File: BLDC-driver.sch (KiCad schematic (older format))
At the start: 80 parts, among them J1 Conn_01x06, J2 Conn_01x06, Q1 FDMS8018, Q2 FDMS8018, Q3 FDMS8018, Q4 FDMS8018, Q5 FDMS8018, Q6 FDMS8018, U1 NCP81151B, U2 STM32F103C8Tx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

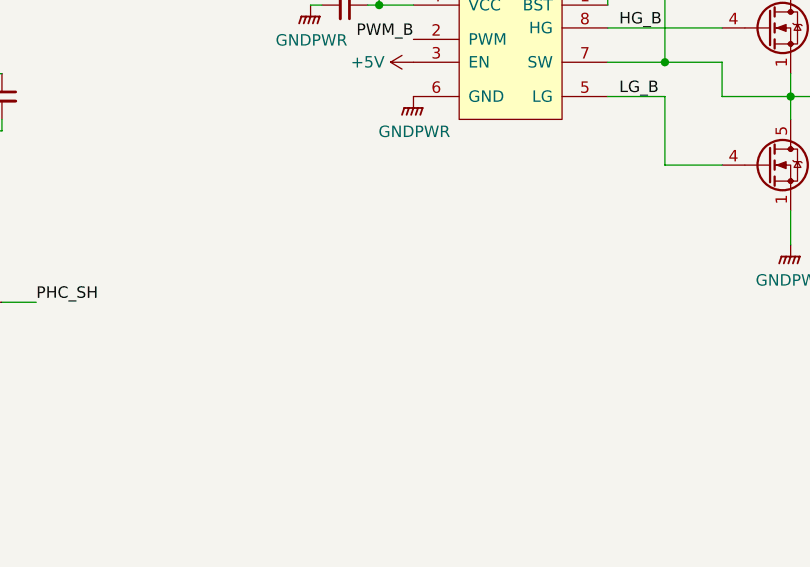
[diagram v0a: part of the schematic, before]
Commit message: add pwm 5v pull up
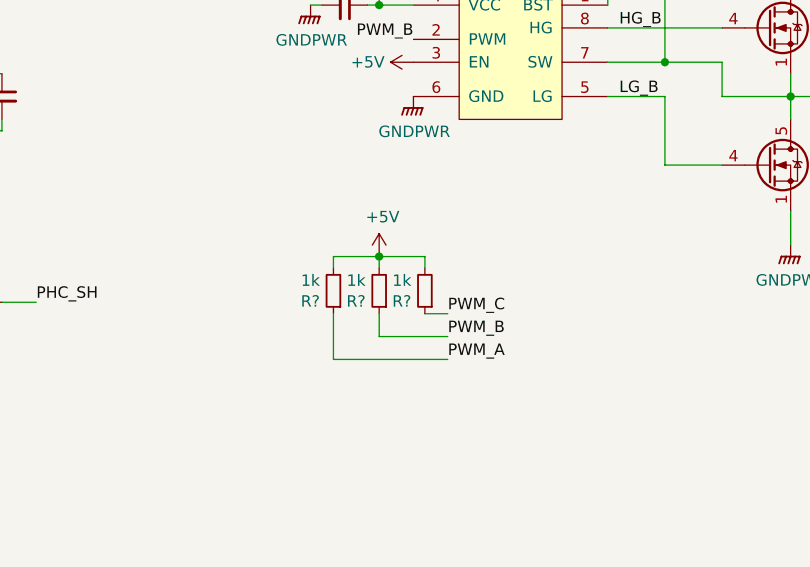
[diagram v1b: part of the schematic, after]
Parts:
- added R? (x3): 1k, Resistor_SMD:R_0402_1005Metric, symbol Device:R_Small
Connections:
- wire segments 294 -> 304
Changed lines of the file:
@@
+	1    0    0    -1
+$EndComp
+Text Label 8400 6250 0    50   ~ 0
+PWM_C
+Text Label 8400 6350 0    50   ~ 0
+PWM_B
+Text Label 8400 6450 0    50   ~ 0
+PWM_A
+$Comp
+L Device:R_Small R?
+U 1 1 5F02E223
+P 8300 6150
+F 0 "R?" H 8359 6196 50  0000 L CNN
+F 1 "1k" H 8359 6105 50  0000 L CNN
+F 2 "Resistor_SMD:R_0402_1005Metric" H 8300 6150 50  0001 C CNN
+F 3 "~" H 8300 6150 50  0001 C CNN
+F 4 "0402" H 8300 6150 50  0001 C CNN "JLCSMT_PKG"
+F 5 "C11702" H 8300 6150 50  0001 C CNN "JLCSMT"
+	1    8300 6150
+	-1   0    0    1
+$EndComp
+Wire Wire Line
+	8400 6250 8300 6250
+$Comp
+L Device:R_Small R?
+U 1 1 5F049AF9
+P 8100 6150
+F 0 "R?" H 8159 6196 50  0000 L CNN
+F 1 "1k" H 8159 6105 50  0000 L CNN
+F 2 "Resistor_SMD:R_0402_1005Metric" H 8100 6150 50  0001 C CNN
+F 3 "~" H 8100 6150 50  0001 C CNN
+F 4 "0402" H 8100 6150 50  0001 C CNN "JLCSMT_PKG"
+F 5 "C11702" H 8100 6150 50  0001 C CNN "JLCSMT"
+	1    8100 6150
+	-1   0    0    1
+$EndComp
+Wire Wire Line
+	8400 6350 8100 6350
+Wire Wire Line
+	8100 6350 8100 6250
+$Comp
+L Device:R_Small R?
+U 1 1 5F064E20
+P 7900 6150
+F 0 "R?" H 7959 6196 50  0000 L CNN
+F 1 "1k" H 7959 6105 50  0000 L CNN
+F 2 "Resistor_SMD:R_0402_1005Metric" H 7900 6150 50  0001 C CNN
+F 3 "~" H 7900 6150 50  0001 C CNN
+F 4 "0402" H 7900 6150 50  0001 C CNN "JLCSMT_PKG"
+F 5 "C11702" H 7900 6150 50  0001 C CNN "JLCSMT"
+	1    7900 6150
+	-1   0    0    1
+$EndComp
+Wire Wire Line
+	7900 6250 7900 6450
+Wire Wire Line
+	7900 6450 8400 6450
+Wire Wire Line
+	7900 6050 7900 6000
+Wire Wire Line
+	7900 6000 8100 6000
+Wire Wire Line
+	8100 6000 8100 6050
+Wire Wire Line
+	8100 6000 8300 6000
+Wire Wire Line
+	8300 6000 8300 6050
+Connection ~ 8100 6000
+$Comp
+L power:+5V #PWR?
+U 1 1 5F0B8419
+P 8100 6000
+F 0 "#PWR?" H 8100 5850 50  0001 C CNN
+F 1 "+5V" H 8115 6173 50  0000 C CNN
+F 2 "" H 8100 6000 50  0001 C CNN
+F 3 "" H 8100 6000 50  0001 C CNN
+	1    8100 6000
 	1    0    0    -1
 $EndComp

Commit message: Add snubbers
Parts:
- added C22, C33, C34: 2.7nF, Capacitor_SMD:C_0402_1005Metric, symbol Device:C_Small
- added R25, R26, R27: 2.2R, Resistor_SMD:R_0402_1005Metric, symbol Device:R_Small
- gave numbers to parts that had none: 3
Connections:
- wire segments 304 -> 316
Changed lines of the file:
@@
 F 1 "NCP81151B" H 8575 1774 50  0000 C CNN
 F 2 "Package_DFN_QFN:DFN-8-1EP_2x2mm_P0.5mm_EP0.9x1.5mm" H 8600 1850 50  0001 C CNN
-F 3 "http://www.farnell.com/datasheets/1878373.pdf" H 8600 1850 50  0001 C CNN
+F 3 "https://www.onsemi.com/pub/Collateral/NCP81151-D.PDF" H 8600 1850 50  0001 C CNN
 	1    8600 1850
 	1    0    0    -1
@@
 F 1 "NCP81151B" H 8675 4574 50  0000 C CNN
 F 2 "Package_DFN_QFN:DFN-8-1EP_2x2mm_P0.5mm_EP0.9x1.5mm" H 8700 4650 50  0001 C CNN
-F 3 "http://www.farnell.com/datasheets/1878373.pdf" H 8700 4650 50  0001 C CNN
+F 3 "https://www.onsemi.com/pub/Collateral/NCP81151-D.PDF" H 8700 4650 50  0001 C CNN
 	1    8700 4650
 	1    0    0    -1
@@
 F 1 "NCP81151B" H 4475 5474 50  0000 C CNN
 F 2 "Package_DFN_QFN:DFN-8-1EP_2x2mm_P0.5mm_EP0.9x1.5mm" H 4500 5550 50  0001 C CNN
-F 3 "http://www.farnell.com/datasheets/1878373.pdf" H 4500 5550 50  0001 C CNN
+F 3 "https://www.onsemi.com/pub/Collateral/NCP81151-D.PDF" H 4500 5550 50  0001 C CNN
 	1    4500 5550
 	1    0    0    -1
@@
 PWM_A
 $Comp
-L Device:R_Small R?
+L Device:R_Small R6
 U 1 1 5F02E223
 P 8300 6150
-F 0 "R?" H 8359 6196 50  0000 L CNN
+F 0 "R6" H 8359 6196 50  0000 L CNN
 F 1 "1k" H 8359 6105 50  0000 L CNN
 F 2 "Resistor_SMD:R_0402_1005Metric" H 8300 6150 50  0001 C CNN
@@
 	8400 6250 8300 6250
 $Comp
-L Device:R_Small R?
+L Device:R_Small R5
 U 1 1 5F049AF9
 P 8100 6150
-F 0 "R?" H 8159 6196 50  0000 L CNN
+F 0 "R5" H 8159 6196 50  0000 L CNN
 F 1 "1k" H 8159 6105 50  0000 L CNN
 F 2 "Resistor_SMD:R_0402_1005Metric" H 8100 6150 50  0001 C CNN
@@
 	8100 6350 8100 6250
 $Comp
-L Device:R_Small R?
+L Device:R_Small R4
 U 1 1 5F064E20
 P 7900 6150
-F 0 "R?" H 7959 6196 50  0000 L CNN
+F 0 "R4" H 7959 6196 50  0000 L CNN
 F 1 "1k" H 7959 6105 50  0000 L CNN
 F 2 "Resistor_SMD:R_0402_1005Metric" H 7900 6150 50  0001 C CNN
@@
 Connection ~ 8100 6000
 $Comp
-L power:+5V #PWR?
+L power:+5V #PWR0128
 U 1 1 5F0B8419
 P 8100 6000
-F 0 "#PWR?" H 8100 5850 50  0001 C CNN
+F 0 "#PWR0128" H 8100 5850 50  0001 C CNN
 F 1 "+5V" H 8115 6173 50  0000 C CNN
 F 2 "" H 8100 6000 50  0001 C CNN
@@
 	1    0    0    -1
 $EndComp
+Text Label 7100 5350 0    50   ~ 0
+PH_B
+Text Label 6800 5350 0    50   ~ 0
+PH_A
+Text Label 7400 5350 0    50   ~ 0
+PH_C
+$Comp
+L Device:R_Small R25
+U 1 1 5F0E37B3
+P 6800 5550
+F 0 "R25" H 6859 5596 50  0000 L CNN
+F 1 "2.2R" H 6859 5505 50  0000 L CNN
+F 2 "Resistor_SMD:R_0402_1005Metric" H 6800 5550 50  0001 C CNN
+F 3 "~" H 6800 5550 50  0001 C CNN
+F 4 "0402" H 6800 5550 50  0001 C CNN "JLCSMT_PKG"
+F 5 "C11702" H 6800 5550 50  0001 C CNN "JLCSMT"
+	1    6800 5550
+	-1   0    0    1
+$EndComp
+$Comp
+L Device:R_Small R26
+U 1 1 5F0E3D45
+P 7100 5550
+F 0 "R26" H 7159 5596 50  0000 L CNN
+F 1 "2.2R" H 7159 5505 50  0000 L CNN
+F 2 "Resistor_SMD:R_0402_1005Metric" H 7100 5550 50  0001 C CNN
+F 3 "~" H 7100 5550 50  0001 C CNN
+F 4 "0402" H 7100 5550 50  0001 C CNN "JLCSMT_PKG"
+F 5 "C11702" H 7100 5550 50  0001 C CNN "JLCSMT"
+	1    7100 5550
+	-1   0    0    1
+$EndComp
+$Comp
+L Device:R_Small R27
+U 1 1 5F0E3E9B
+P 7400 5550
+F 0 "R27" H 7459 5596 50  0000 L CNN
+F 1 "2.2R" H 7459 5505 50  0000 L CNN
+F 2 "Resistor_SMD:R_0402_1005Metric" H 7400 5550 50  0001 C CNN
+F 3 "~" H 7400 5550 50  0001 C CNN
+F 4 "0402" H 7400 5550 50  0001 C CNN "JLCSMT_PKG"
+F 5 "C11702" H 7400 5550 50  0001 C CNN "JLCSMT"
+	1    7400 5550
+	-1   0    0    1
+$EndComp
+Wire Wire Line
+	6800 5450 6800 5350
+Wire Wire Line
+	7100 5450 7100 5350
+Wire Wire Line
+	7400 5350 7400 5450
+$Comp
+L Device:C_Small C22
+U 1 1 5F138F19
+P 6800 5800
+F 0 "C22" H 6600 5900 50  0000 C CNN
+F 1 "2.7nF" H 6600 5850 50  0000 C CNN
+F 2 "Capacitor_SMD:C_0402_1005Metric" H 6800 5800 50  0001 C CNN
+F 3 "~" H 6800 5800 50  0001 C CNN
+F 4 "C1525" H 6800 5800 50  0001 C CNN "JLCSMT"
+F 5 "0402" H 6800 5800 50  0001 C CNN "JLCSMT_PKG"
+	1    6800 5800
+	1    0    0    -1
+$EndComp
+Wire Wire Line
+	6800 5700 6800 5650
+$Comp
+L Device:C_Small C33
+U 1 1 5F15D0C0
+P 7100 5800
+F 0 "C33" H 6900 5900 50  0000 C CNN
+F 1 "2.7nF" H 6900 5850 50  0000 C CNN
+F 2 "Capacitor_SMD:C_0402_1005Metric" H 7100 5800 50  0001 C CNN
+F 3 "~" H 7100 5800 50  0001 C CNN
+F 4 "C1525" H 7100 5800 50  0001 C CNN "JLCSMT"
+F 5 "0402" H 7100 5800 50  0001 C CNN "JLCSMT_PKG"
+	1    7100 5800
+	1    0    0    -1
+$EndComp
+$Comp
+L Device:C_Small C34
+U 1 1 5F15D486
+P 7400 5800
+F 0 "C34" H 7200 5900 50  0000 C CNN
+F 1 "2.7nF" H 7200 5850 50  0000 C CNN
+F 2 "Capacitor_SMD:C_0402_1005Metric" H 7400 5800 50  0001 C CNN
+F 3 "~" H 7400 5800 50  0001 C CNN
+F 4 "C1525" H 7400 5800 50  0001 C CNN "JLCSMT"
+F 5 "0402" H 7400 5800 50  0001 C CNN "JLCSMT_PKG"
+	1    7400 5800
+	1    0    0    -1
+$EndComp
+$Comp
+L power:GNDPWR #PWR0129
+U 1 1 5F15D96A
+P 7100 6000
+F 0 "#PWR0129" H 7100 5800 50  0001 C CNN
+F 1 "GNDPWR" H 7104 5846 50  0000 C CNN
+F 2 "" H 7100 5950 50  0001 C CNN
+F 3 "" H 7100 5950 50  0001 C CNN
+	1    7100 6000
+	1    0    0    -1
+$EndComp
+Wire Wire Line
+	7100 6000 7100 5950
+Wire Wire Line
+	7100 5950 7400 5950
+Wire Wire Line
+	7400 5950 7400 5900
+Connection ~ 7100 5950
+Wire Wire Line
+	7100 5950 7100 5900
+Wire Wire Line
+	6800 5900 6800 5950
+Wire Wire Line
+	6800 5950 7100 5950
+Wire Wire Line
+	7400 5650 7400 5700
+Wire Wire Line
+	7100 5650 7100 5700
 $EndSCHEMATC

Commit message: Revision 2 update
Move current shunts to low side. I have encountered smoke from current
amplifiers when working @ 20V.
Adapt to STM32L4xxCBT mcu.
Add snubbers and resistance to gate drivers to reduce ringing due to
very fast switching.
Add RS485 interface instead of CAN
Route ENABLE signal to gate drivers
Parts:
- removed D4, D5, D6: 30V, Diode_SMD:D_SOD-323, symbol Device:D_Schottky_Small
- removed U3: MAX3051, Package_TO_SOT_SMD:SOT-23-8, symbol Interface_UART:MAX3051
- added C35, C36, C37: 100nF, Capacitor_SMD:C_0402_1005Metric, symbol Device:C_Small
- added NT2, NT3: Net-Tie_2, NetTie:NetTie-2_SMD_Pad0.5mm, symbol Device:Net-Tie_2
- added Q7: BC807, Package_TO_SOT_SMD:SOT-23, symbol Transistor_BJT:BC807
- added R28, R29, R30: 10, Resistor_SMD:R_0402_1005Metric, symbol Device:R_Small
- added R31, R32: 0, Resistor_SMD:R_0603_1608Metric, symbol Device:R_Small
- added R33, R34: 1k, Resistor_SMD:R_0402_1005Metric, symbol Device:R_Small
- added R35, R36, R37: 1, Resistor_SMD:R_0402_1005Metric, symbol Device:R_Small
- added SB1: 0, Resistor_SMD:R_0402_1005Metric, symbol Device:R_Small
- added U11: SN75176AD, Package_SO:SOIC-8_3.9x4.9mm_P1.27mm, symbol Interface_UART:SN75176AD
- C13, C18, C23, C28, C29, C4, C5, C6, C7, C9: footprint Capacitor_SMD:C_0603_1608Metric -> Capacitor_SMD:C_0402_1005Metric; JLCSMT C14663 -> C1525; JLCSMT_PKG 0603 -> 0402
- C14, C19, C24, C8: value 4.7uF -> 1uF; footprint Capacitor_SMD:C_0603_1608Metric -> Capacitor_SMD:C_0402_1005Metric; JLCSMT C19666 -> C52923; JLCSMT_PKG 0603 -> 0402
- C22, C33, C34: value 2.7nF -> 22nF; JLCSMT C1525 -> C1532
- C31, C32: value 100nF -> 4.7nF; JLCSMT C1525 -> C1538
- R1, R10, R11, R13: footprint Resistor_SMD:R_0603_1608Metric -> Resistor_SMD:R_0402_1005Metric; JLCSMT C25804 -> C25744; JLCSMT_PKG 0603 -> 0402
- R12, R7: footprint Resistor_SMD:R_0603_1608Metric -> Resistor_SMD:R_0402_1005Metric; JLCSMT C25803 -> C25741; JLCSMT_PKG 0603 -> 0402
- R16: value 120R -> 100; footprint Resistor_SMD:R_0603_1608Metric -> Resistor_SMD:R_0402_1005Metric; JLCSMT C22787 -> C25076; JLCSMT_PKG 0603 -> 0402
- R19, R20: value 2.2k -> 1k; JLCSMT C25879 -> C11702
- R2, R3: JLCSMT (none) -> C4190
- R21: value 2.2k -> 100; JLCSMT C25879 -> C25076
- R22: value 2.2k -> 0; footprint Resistor_SMD:R_0402_1005Metric -> Resistor_SMD:R_0603_1608Metric; JLCSMT C25879 -> C21189; JLCSMT_PKG 0402 -> 0603
- R23, R24: value 1k -> 100; JLCSMT C11702 -> C25076
- R25, R26, R27: value 2.2R -> 1R; JLCSMT C11702 -> C25086
- R9: value 5.6k -> 6.2k; JLCSMT C23189 -> C4260
- U2: value STM32F103C8Tx -> STM32L412CB
- U6: JLCSMT (none) -> C14259; JLCSMT_PKG (none) -> TSOT-23-6
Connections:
- net labels added: 485A, 485B, ENBL, PHB_GND, PHC_GND, U1_DE, U1_RX, U1_TX, VREF_OUT
- net labels removed: CANH, CANL, PB3, PB6, PB7
- wire segments 316 -> 322
- no-connect marks 0 -> 2
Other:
- note added: "Place SB1 if no opamp"
- note added: "Snubbers"
- note added: "[OD]"
- moved on the sheet: C22, C28, C31, C32, C33, C34, R14, R15, R23, R24, R25, R26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

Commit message: Add MPNs for some parts
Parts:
- D7: value D_TVS -> SMAJ24A; MPN (none) -> SMAJ24A-E3/61
- NTC1: MPN (none) -> NCU18XH103F60RB
- R14, R15: MPN (none) -> PMR25HZPFV1L00; URL (none) -> https://lt.farnell.com/rohm/pmr25hzpfv1l00/current-sense-re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
- U1, U4, U5: MPN (none) -> NCP81151MNTBG; URL (none) -> https://lt.farnell.com/on-semiconductor/ncp81151mntbg/mosfe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
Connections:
- no-connect marks 2 -> 10
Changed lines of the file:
@@
 encoding utf-8
 Sheet 1 1
-Title ""
+Title "BLDC FOC Servo"
 Date ""
 Rev ""
-Comp ""
+Comp "Walmis"
 Comment1 ""
 Comment2 ""
@@
 F 2 "Package_DFN_QFN:DFN-8-1EP_2x2mm_P0.5mm_EP0.9x1.5mm" H 8600 1850 50  0001 C CNN
 F 3 "https://www.onsemi.com/pub/Collateral/NCP81151-D.PDF" H 8600 1850 50  0001 C CNN
+F 4 "NCP81151MNTBG" H 8600 1850 50  0001 C CNN "MPN"
+F 5 "https://lt.farnell.com/on-semiconductor/ncp81151mntbg/mosfet-driver-dual-high-low-dfn/dp/2627993?st=ncp811" H 8600 1850 50  0001 C CNN "URL"
 	1    8600 1850
 	1    0    0    -1
@@
 F 2 "Package_DFN_QFN:DFN-8-1EP_2x2mm_P0.5mm_EP0.9x1.5mm" H 8700 4650 50  0001 C CNN
 F 3 "https://www.onsemi.com/pub/Collateral/NCP81151-D.PDF" H 8700 4650 50  0001 C CNN
+F 4 "NCP81151MNTBG" H 8700 4650 50  0001 C CNN "MPN"
+F 5 "https://lt.farnell.com/on-semiconductor/ncp81151mntbg/mosfet-driver-dual-high-low-dfn/dp/2627993?st=ncp811" H 8700 4650 50  0001 C CNN "URL"
 	1    8700 4650
 	1    0    0    -1
@@
 F 2 "Package_DFN_QFN:DFN-8-1EP_2x2mm_P0.5mm_EP0.9x1.5mm" H 4500 5550 50  0001 C CNN
 F 3 "https://www.onsemi.com/pub/Collateral/NCP81151-D.PDF" H 4500 5550 50  0001 C CNN
+F 4 "NCP81151MNTBG" H 4500 5550 50  0001 C CNN "MPN"
+F 5 "https://lt.farnell.com/on-semiconductor/ncp81151mntbg/mosfet-driver-dual-high-low-dfn/dp/2627993?st=ncp811" H 4500 5550 50  0001 C CNN "URL"
 	1    4500 5550
 	1    0    0    -1
@@
 F 2 "Resistor_SMD:R_0603_1608Metric" H 6700 1450 50  0001 C CNN
 F 3 "~" H 6700 1450 50  0001 C CNN
+F 4 "NCU18XH103F60RB" H 6700 1400 50  0001 C CNN "MPN"
 	1    6700 1400
 	1    0    0    -1
@@
 F 2 "Resistor_SMD:R_1210_3225Metric" V 9830 6050 50  0001 C CNN
 F 3 "~" H 9900 6050 50  0001 C CNN
+F 4 "PMR25HZPFV1L00" H 9900 6050 50  0001 C CNN "MPN"
+F 5 "https://lt.farnell.com/rohm/pmr25hzpfv1l00/current-sense-res-0r001-1-1-w/dp/2696414" H 9900 6050 50  0001 C CNN "URL"
 	1    9900 6050
 	-1   0    0    1
@@
 F 2 "Resistor_SMD:R_1210_3225Metric" V 5630 6900 50  0001 C CNN
 F 3 "~" H 5700 6900 50  0001 C CNN
+F 4 "PMR25HZPFV1L00" H 5700 6900 50  0001 C CNN "MPN"
+F 5 "https://lt.farnell.com/rohm/pmr25hzpfv1l00/current-sense-res-0r001-1-1-w/dp/2696414" H 5700 6900 50  0001 C CNN "URL"
 	1    5700 6900
 	-1   0    0    1
@@
 P 9450 1650
 F 0 "D7" V 9404 1730 50  0000 L CNN
-F 1 "D_TVS" V 9495 1730 50  0000 L CNN
+F 1 "SMAJ24A" V 9495 1730 50  0000 L CNN
 F 2 "Diode_SMD:D_SMB" H 9450 1650 50  0001 C CNN
 F 3 "~" H 9450 1650 50  0001 C CNN
+F 4 "SMAJ24A-E3/61" H 9450 1650 50  0001 C CNN "MPN"
 	1    9450 1650
 	0    1    1    0
@@
 	0    1    1    0
 $EndComp
+NoConn ~ 2550 3150
+NoConn ~ 2550 3250
+NoConn ~ 2550 3350
+NoConn ~ 2550 3550
+NoConn ~ 2550 3650
+NoConn ~ 2550 3750
+NoConn ~ 2550 4750
+NoConn ~ 2550 4850
 $EndSCHEMATC
